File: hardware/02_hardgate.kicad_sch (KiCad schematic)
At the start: 20 parts, among them Q1 MMBT3906, Q2 MMBT3906, U2 TPS26600PWPR

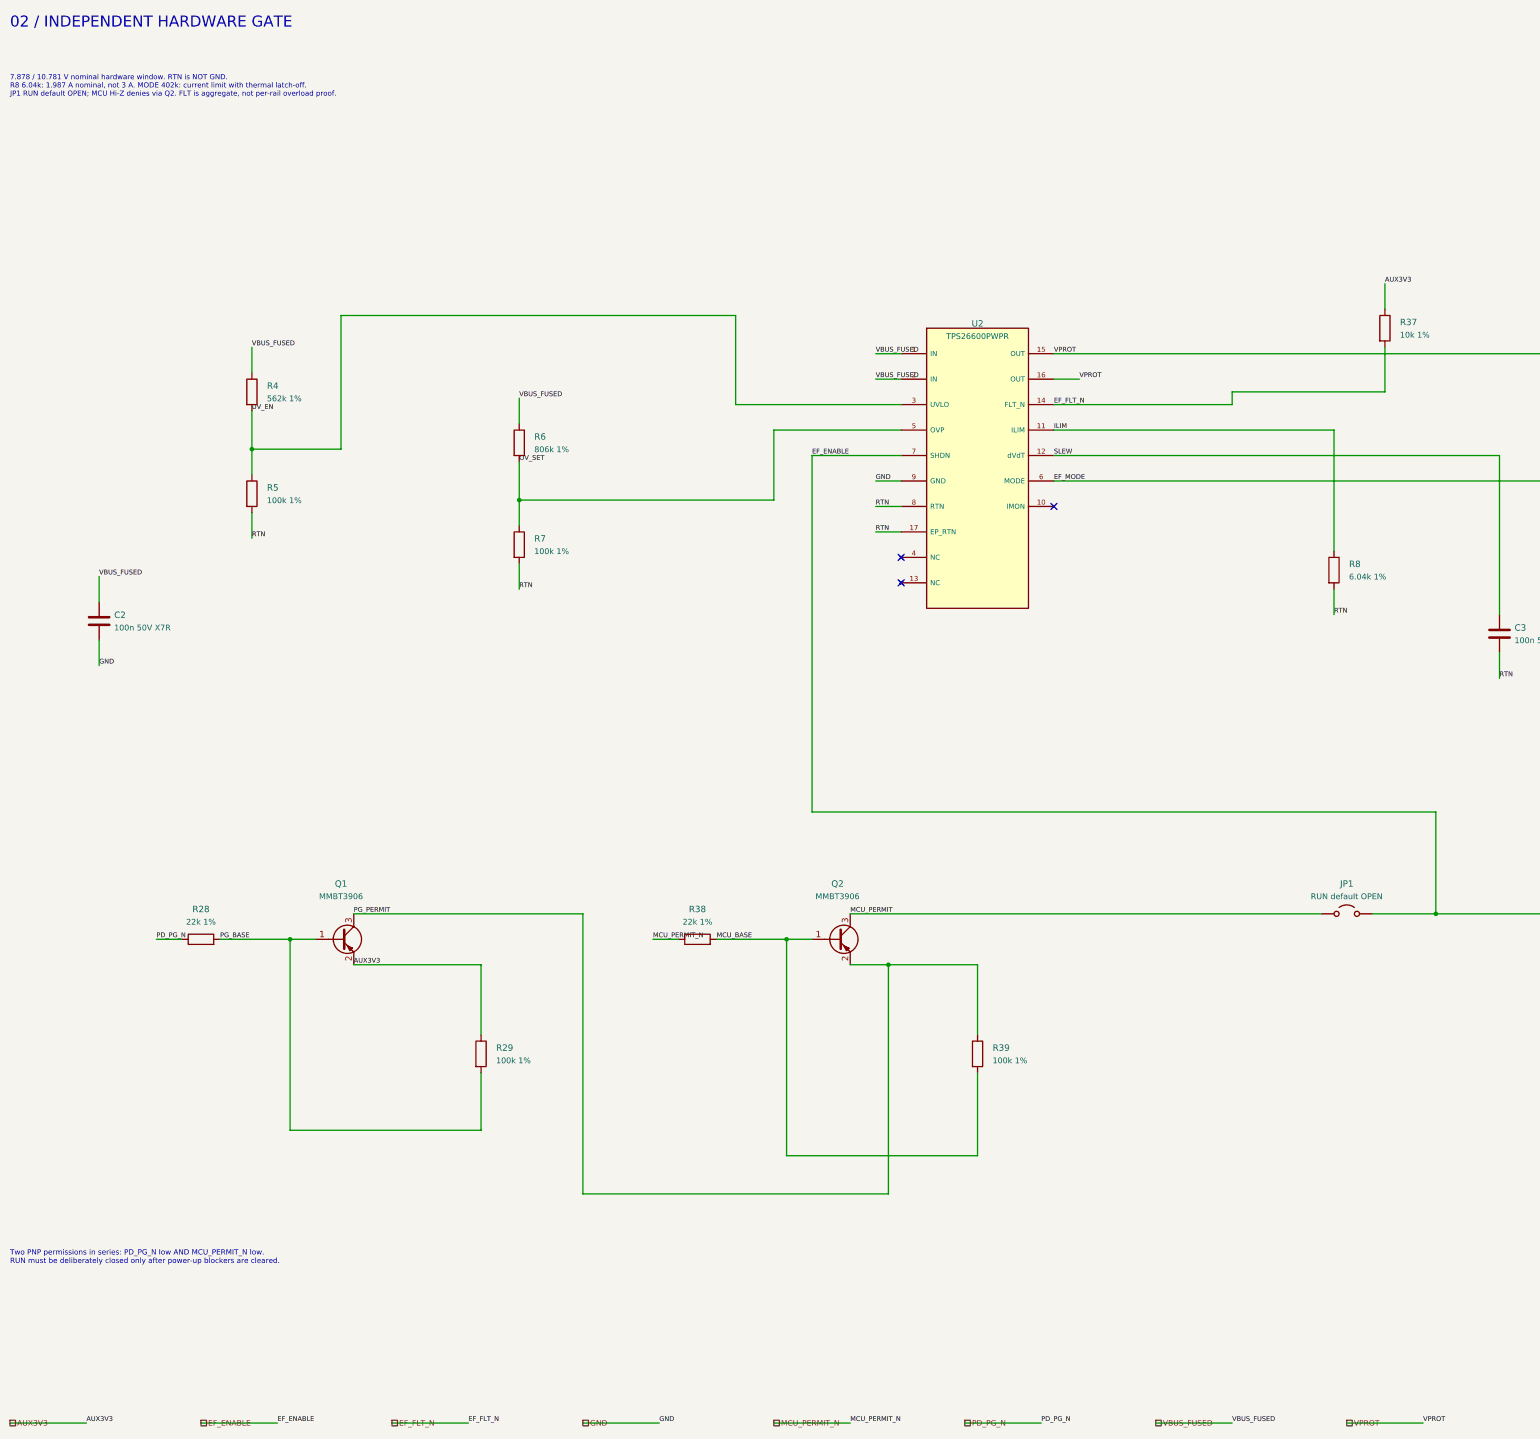
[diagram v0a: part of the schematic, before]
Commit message: Replace MCU diagnostics with optional rail-sense IDC and single 5 V power LED
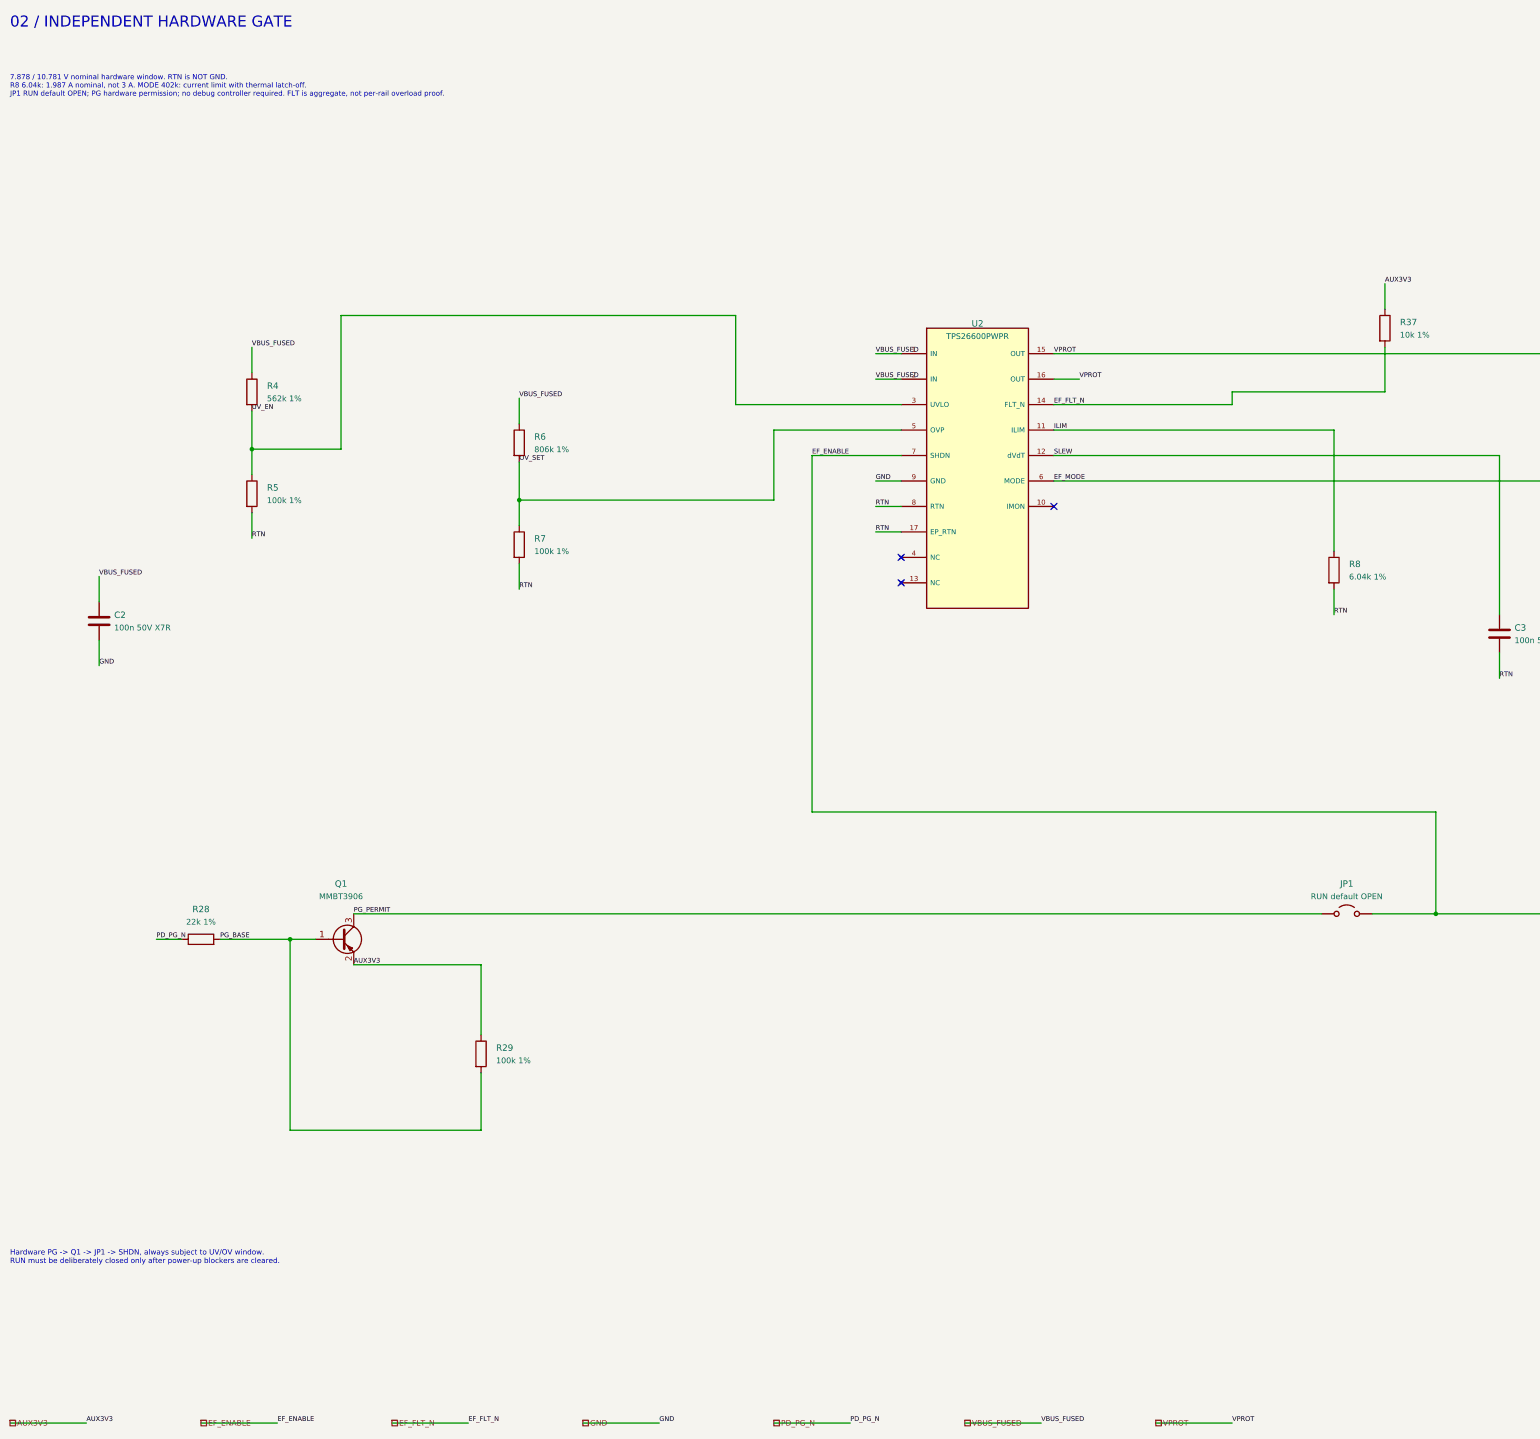
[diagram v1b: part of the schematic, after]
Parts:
- removed Q2: MMBT3906, BigModular:SOT-23, symbol BigModular:Transistor_BJT_MMBT3906
- removed R38: 22k 1%, BigModular:R_0603_1608Metric, symbol BigModular:Device_R
- removed R39: 100k 1%, BigModular:R_0603_1608Metric, symbol BigModular:Device_R
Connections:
- net MCU_PERMIT is gone; now on net PG_PERMIT: JP1.1 (A)
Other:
- note added: "7.878 / 10.781 V nominal hardware window. RTN is NOT GND. R8 6.04k: 1.987 A nominal, not 3 A. MODE 402k: current limit with thermal latch-off. JP1 RUN default OPEN; PG hardware permission; no debug controller required. FLT is aggregate, not per-rail overload proof."
- note added: "Hardware PG -> Q1 -> JP1 -> SHDN, always subject to UV/OV window. RUN must be deliberately closed only after power-up blockers are cleared."
- note removed: "7.878 / 10.781 V nominal hardware window. RTN is NOT GND. R8 6.04k: 1.987 A nominal, not 3 A. MODE 402k: current limit with thermal latch-off. JP1 RUN default OPEN; MCU Hi-Z denies via Q2. FLT is aggregate, not per-rail overload proof."
- note removed: "Two PNP permissions in series: PD_PG_N low AND MCU_PERMIT_N low. RUN must be deliberately closed only after power-up blockers are cleared."

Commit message: Simplify V1 power architecture, remove auxiliary sensing and obsolete documentation, enable autonomous protected start and reset button
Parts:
- removed JP1: RUN default OPEN, BigModular:SolderJumper-2_P1.3mm_Open_Pad1.0x1.5mm, symbol BigModular:Jumper_Jumper_2_Open
- removed Q1: MMBT3906, BigModular:SOT-23, symbol BigModular:Transistor_BJT_MMBT3906
- removed R28: 22k 1%, BigModular:R_0603_1608Metric, symbol BigModular:Device_R
- removed R29: 100k 1%, BigModular:R_0603_1608Metric, symbol BigModular:Device_R
- removed R30, R37: 10k 1%, BigModular:R_0603_1608Metric, symbol BigModular:Device_R
- added SW1: TL3340AF160QG, BigModular:SW_TL3340AF160QG_HandSolder, symbol BigModular:TL3340AF160QG
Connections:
- net RTN: now also SW1.2 (NO)
- net EF_ENABLE renamed EF_SHDN
- net EF_SHDN: now also SW1.1 (COMMON), SW1.3 (COMMON)
- net EF_FLT_N: no longer names the net of U2.14 (FLT_N)
- net VBUS_FUSED renamed VIN9
- no-connect marks 3 -> 5
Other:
- note added: "02 / AUTONOMOUS HARDWARE WINDOW AND RETRY"
- note added: "SW1 PRESS: SHDN -> RTN, eFuse OFF; RELEASE: internal 2.0..3.4 V bias retries. No AUX/PG/JP1 or external permission. UV/OV/current/thermal protection always applies. Bucks use their own internal EN pullups, not this weak SHDN bias."
- note added: "UV rising 7.878 V / OV rising 10.781 V nominal; hysteresis applies. RTN is NOT GND. SHDN self-biases internally; SW1 shorts SHDN to RTN while pressed, release resets/retries. R8 6.04k: 1.987 A nominal. MODE 402k: current limit with thermal latch-off. No PG/MCU permission."
- note removed: "02 / INDEPENDENT HARDWARE GATE"
- note removed: "7.878 / 10.781 V nominal hardware window. RTN is NOT GND. R8 6.04k: 1.987 A nominal, not 3 A. MODE 402k: current limit with thermal latch-off. JP1 RUN default OPEN; PG hardware permission; no debug controller required. FLT is aggregate, not per-rail overload proof."
- note removed: "Hardware PG -> Q1 -> JP1 -> SHDN, always subject to UV/OV window. RUN must be deliberately closed only after power-up blockers are cleared."
- title: Big Modular - Independent hardware gate -> Big Modular - Autonomous hardware window and retry

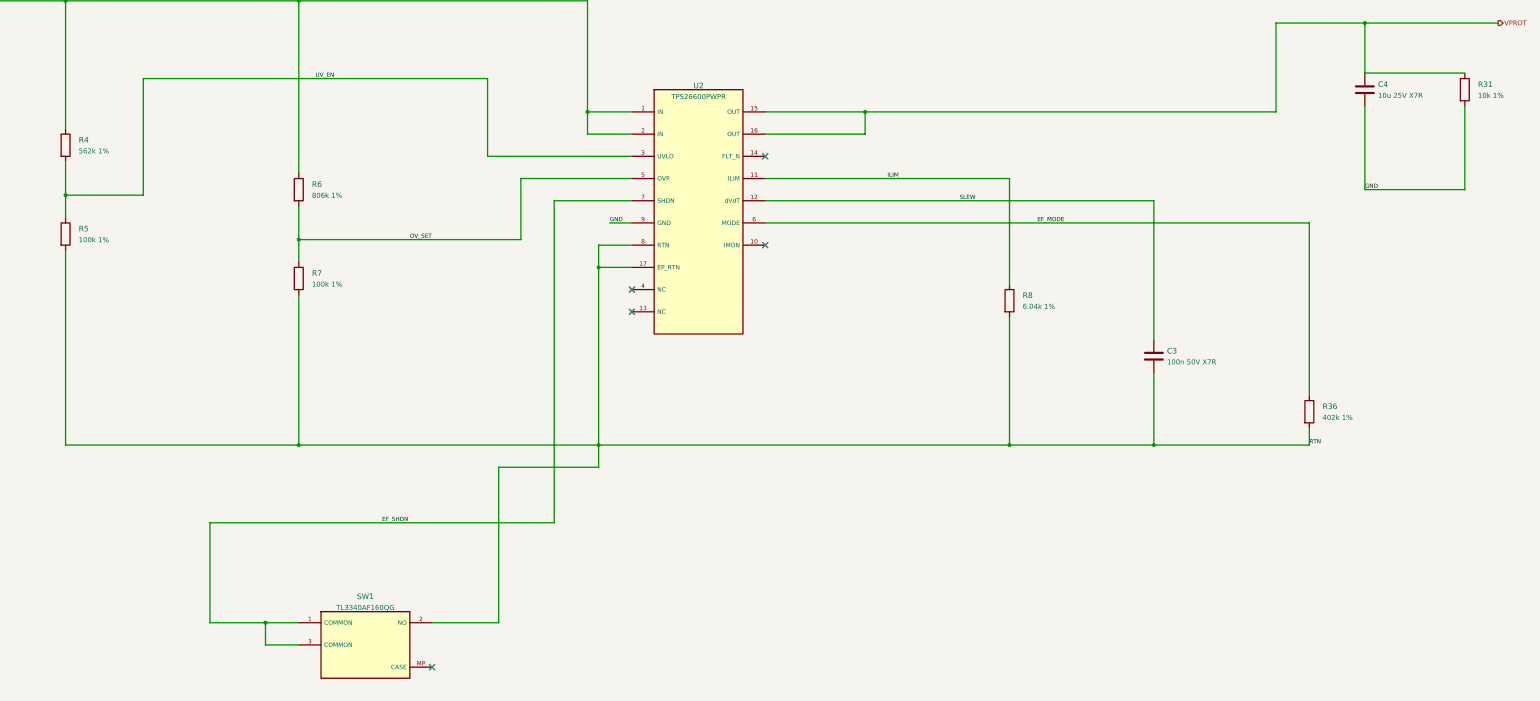
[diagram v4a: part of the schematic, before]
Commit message: Complete four-layer routing, adopt proven HRO USB-C and release checked fabrication files
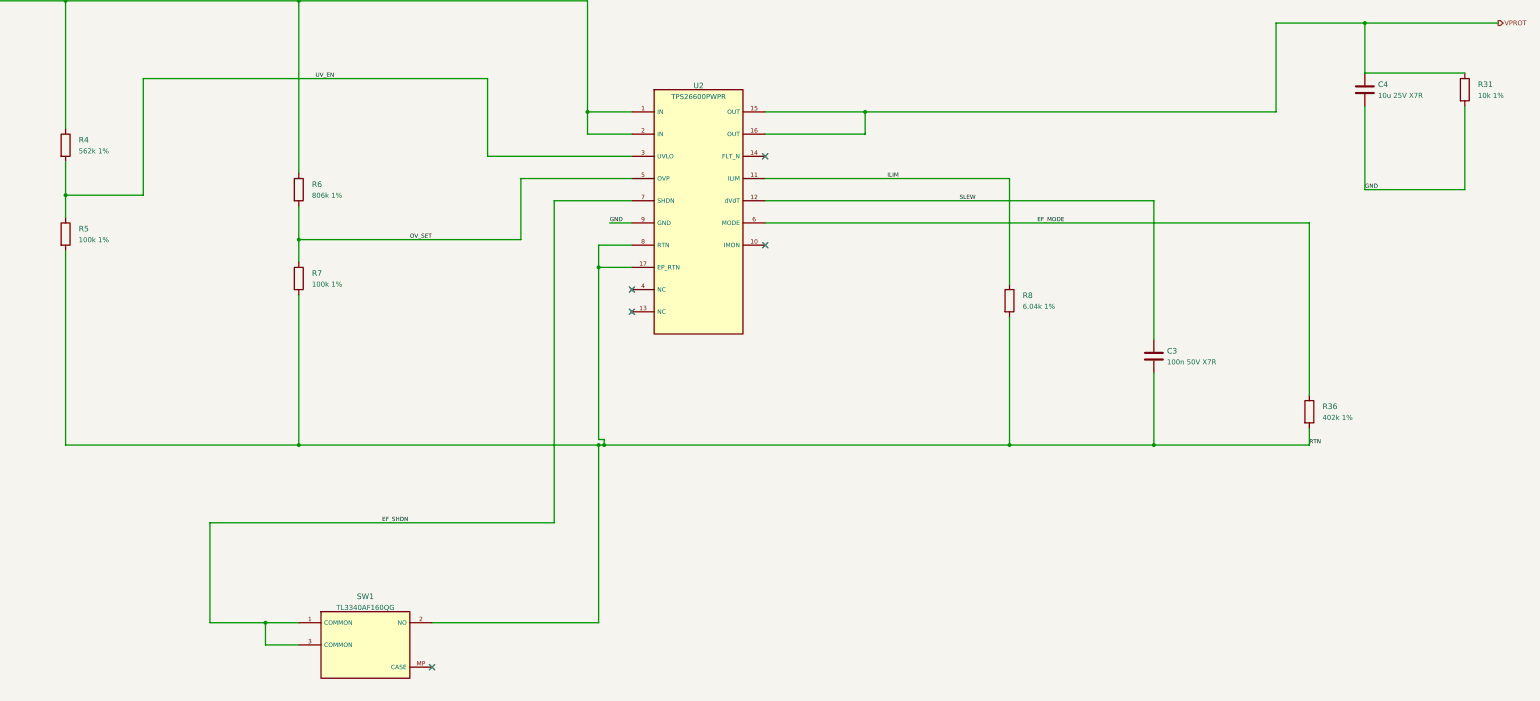
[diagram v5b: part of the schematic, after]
